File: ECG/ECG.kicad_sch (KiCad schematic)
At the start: 91 parts, among them J1 Conn_01x03, J10 Socket 1x15, J11 Shunt block, J12 Shunt block, J13 Shunt block, J14 Shunt block, J15 Shunt block, J16 Shunt block, J17 Conn_02x04_Odd_Even, J2 Conn_01x03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

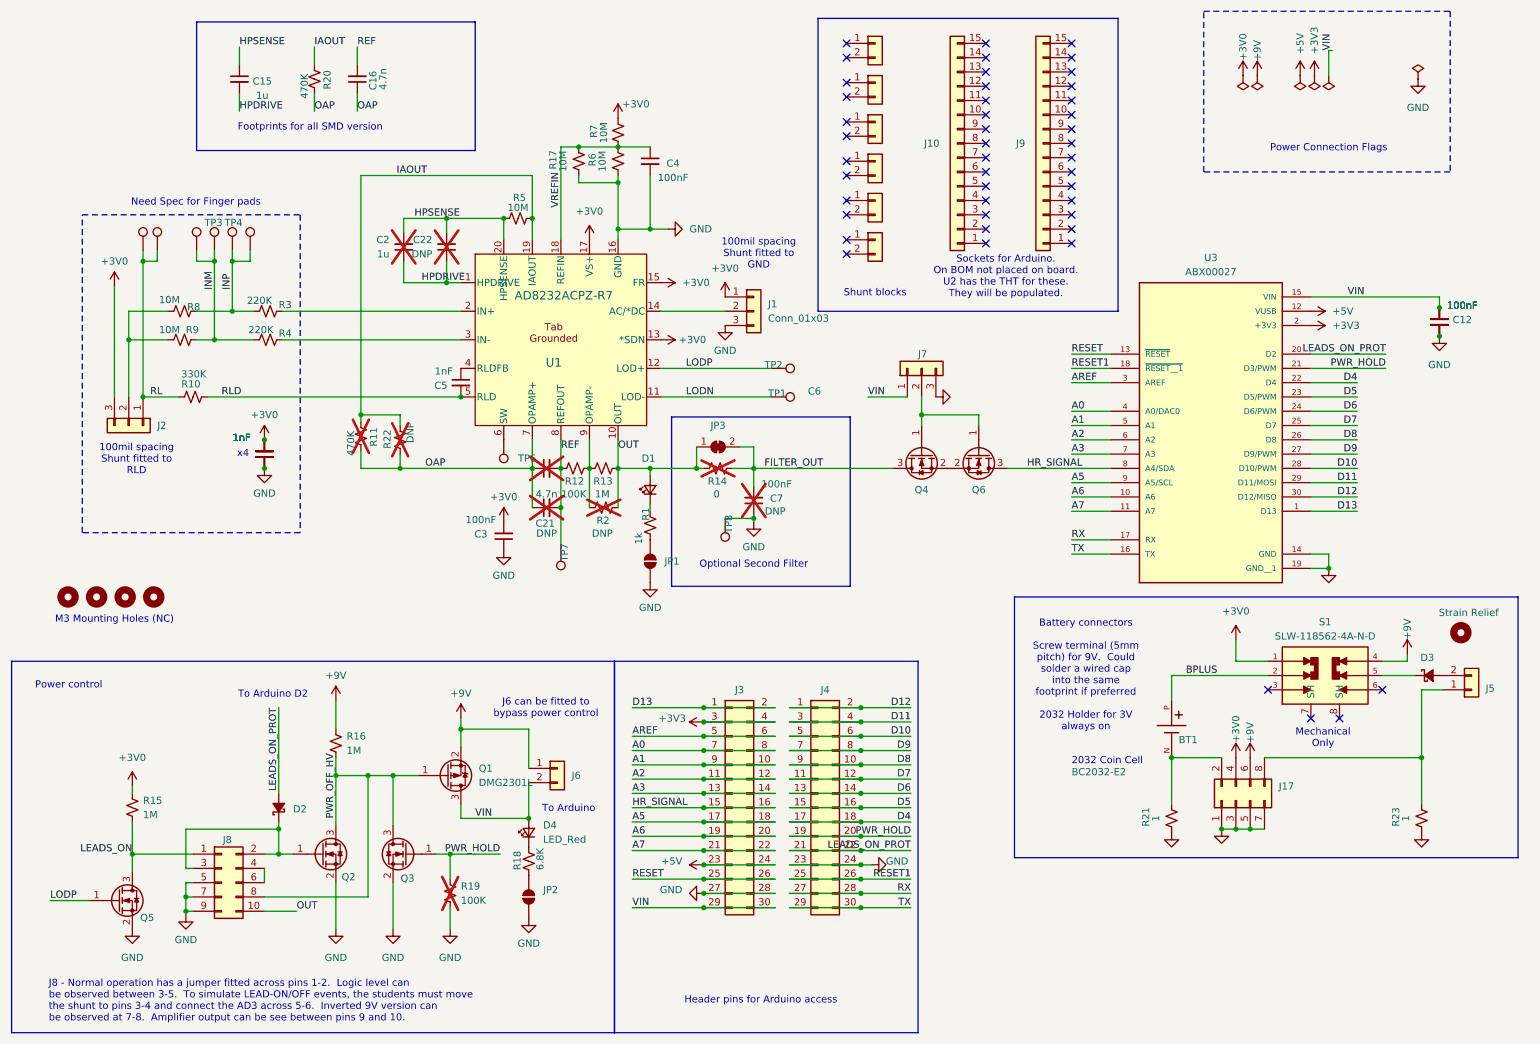
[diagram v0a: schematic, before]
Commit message: Add op amp buffer to pwr_off_hv to allow monitoring with the relatively low input impedance of the AD3
Work on #25

Probably need to look for a CMOS op-amp.  This one pulls
600nA input bias which will likely turn on the pfet and
power up the nano all the time...
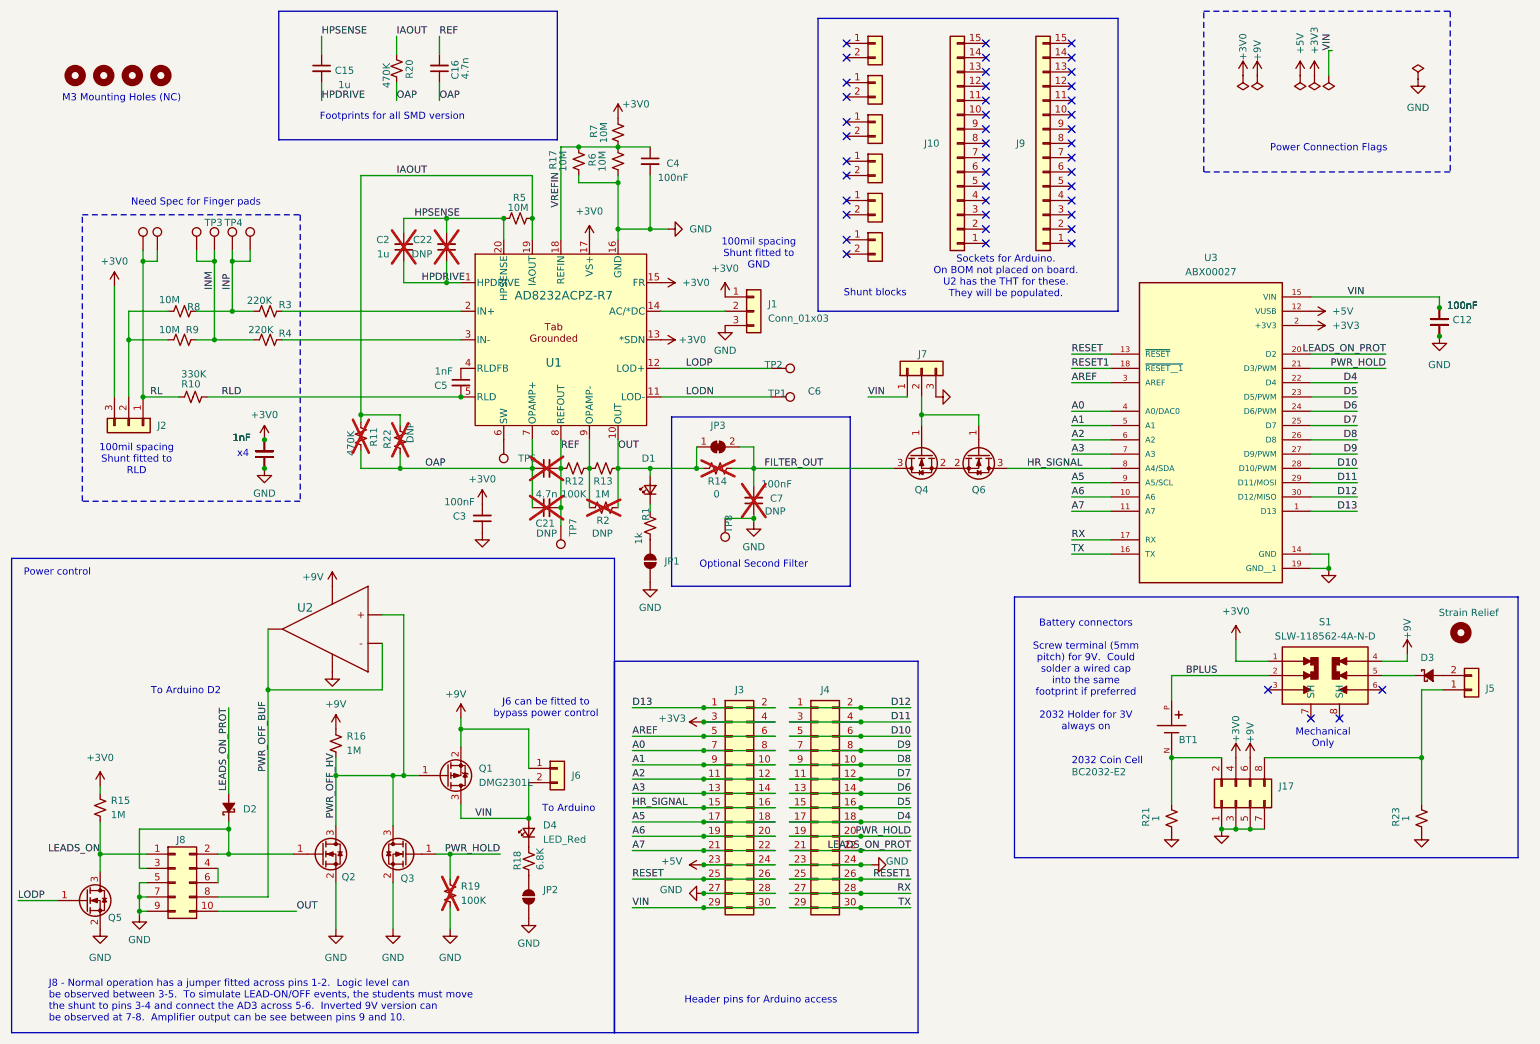
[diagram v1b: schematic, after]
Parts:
- added U2: MIC920YC5-TR, StockedComponents:SC-70_C5_MCH, symbol StockedComponents:MIC920YC5-TR
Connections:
- net +9V: now also U2.5 (V+)
- net GND: now also U2.2 (V-)
- net PWR_OFF_HV: now also U2.1 (IN+); no longer J8.8 (Pin_8)
- new net PWR_OFF_BUF: J8.8 (Pin_8), U2.3 (IN-), U2.4 (OUT)
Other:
- moved on the sheet: C15, C16, C3, D2, J8, Q5, R15, R20, TP7

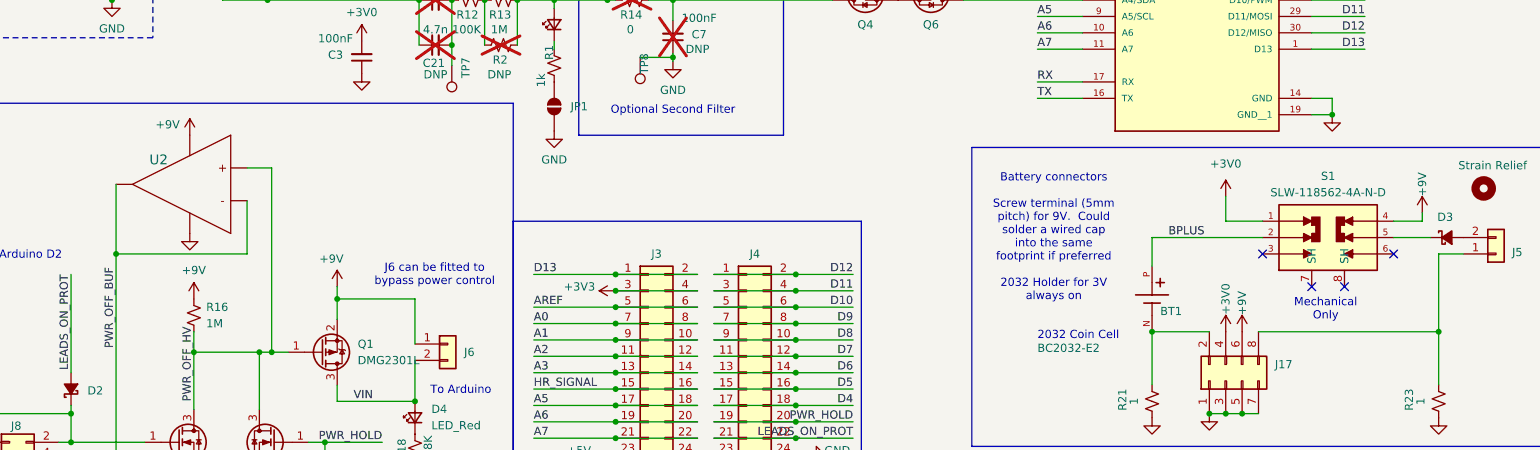
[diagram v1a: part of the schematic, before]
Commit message: Start looking at footprints and placements.
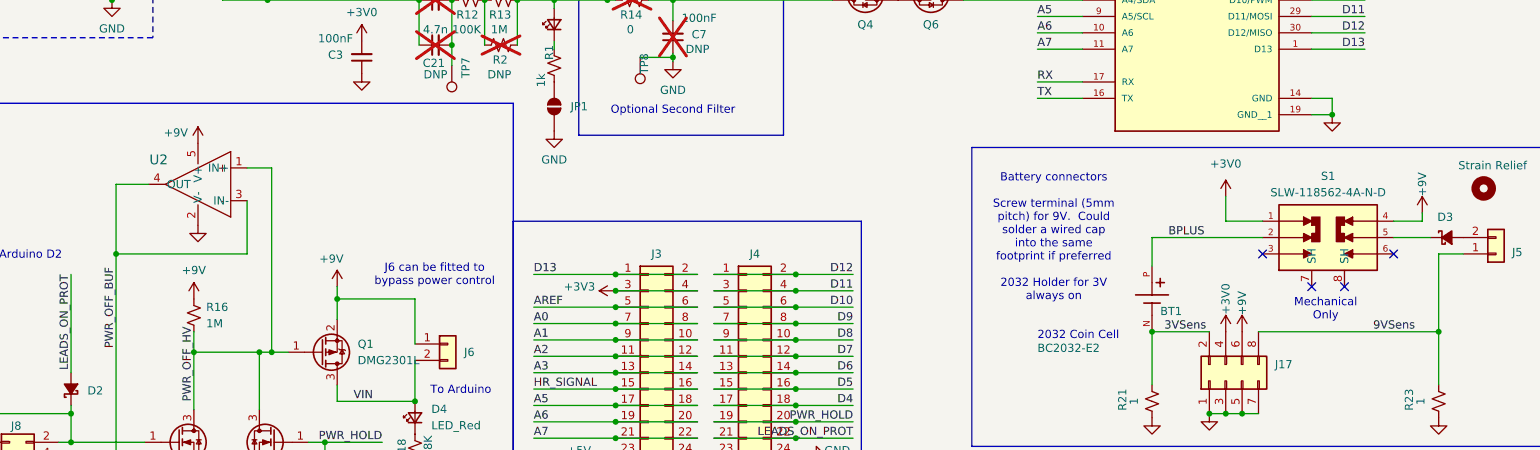
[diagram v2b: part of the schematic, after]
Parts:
- J17: footprint (none) -> Connector_PinHeader_2.54mm:PinHeader_2x04_P2.54mm_Vertical
- J3, J4: footprint (none) -> Connector_PinHeader_2.54mm:PinHeader_2x15_P2.54mm_Vertical
- U2: footprint StockedComponents:SC-70_C5_MCH -> SC-70_C5_MCH
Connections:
- net 9VSens: now reaches J17.8 (Pin_8), J5.1 (Pin_1), R23.1
- net 3VSens: now reaches BT1.N, J17.2 (Pin_2), R21.1
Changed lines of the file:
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@@
 	(wire
 		(pts
+			(xy 61.595 123.825) (xy 66.675 123.825)
+		)
+		(stroke
+			(width 0)
+			(type default)
+		)
+	)
+	(wire
+		(pts
 			(xy 38.735 168.91) (xy 40.005 168.91)
 		)
@@
 		)
 	)
+	(label "9VSens"
+		(at 256.54 146.685 0)
+		(effects
+			(font
+				(size 1.27 1.27)
+			)
+			(justify left bottom)
+		)
+	)
 	(label "RL"
 		(at 40.64 82.55 0)
@@
 		)
 	)
+	(label "3VSens"
+		(at 224.155 146.685 0)
+		(effects
+			(font
+				(size 1.27 1.27)
+			)
+			(justify left bottom)
+		)
+	)
 	(label "PWR_HOLD"
 		(at 260.35 77.47 180)
@@
 			)
 		)
-		(property "Footprint" ""
+		(property "Footprint" "Connector_PinHeader_2.54mm:PinHeader_2x15_P2.54mm_Vertical"
 			(at 144.145 155.575 0)
 			(effects
@@
 			)
 		)
-		(property "Footprint" ""
+		(property "Footprint" "Connector_PinHeader_2.54mm:PinHeader_2x04_P2.54mm_Vertical"
 			(at 233.68 154.305 0)
 			(effects
@@
 	(symbol
 		(lib_id "power:+9V")
-		(at 73.025 116.205 0)
+		(at 74.295 117.475 0)
 		(mirror y)
 		(unit 1)
@@
 		(dnp no)
 		(property "Reference" "#PWR045"
-			(at 73.025 120.015 0)
+			(at 74.295 121.285 0)
 			(effects
 				(font
@@
 		)
 		(property "Value" "+9V"
-			(at 69.596 114.554 0)
+			(at 70.866 115.824 0)
 			(effects
 				(font
@@
 		)
 		(property "Footprint" ""
-			(at 73.025 116.205 0)
+			(at 74.295 117.475 0)
 			(effects
 				(font
@@
 		)
 		(property "Datasheet" ""
-			(at 73.025 116.205 0)
+			(at 74.295 117.475 0)
 			(effects
 				(font
@@
 		)
 		(property "Description" "Power symbol creates a global label with name \"+9V\""
-			(at 73.025 116.205 0)
+			(at 74.295 117.475 0)
 			(effects
 				(font
@@
 			)
 		)
-		(property "Footprint" "StockedComponents:SC-70_C5_MCH"
+		(property "Footprint" "SC-70_C5_MCH"
 			(at 86.995 121.285 0)
 			(effects
@@
 	(symbol
 		(lib_id "power:GND")
-		(at 73.025 131.445 0)
+		(at 74.295 130.175 0)
 		(unit 1)
 		(exclude_from_sim no)
@@
 		(fields_autoplaced yes)
 		(property "Reference" "#PWR046"
-			(at 73.025 137.795 0)
+			(at 74.295 136.525 0)
 			(effects
 				(font
@@
 		)
 		(property "Value" "GND"
-			(at 73.025 135.89 0)
+			(at 74.295 134.62 0)
 			(effects
 				(font
@@
 		)
 		(property "Footprint" ""
-			(at 73.025 131.445 0)
+			(at 74.295 130.175 0)
 			(effects
 				(font
@@
 		)
 		(property "Datasheet" ""
-			(at 73.025 131.445 0)
+			(at 74.295 130.175 0)
 			(effects
 				(font
@@
 		)
 		(property "Description" "Power symbol creates a global label with name \"GND\" , ground"
-			(at 73.025 131.445 0)
+			(at 74.295 130.175 0)
 			(effects
 				(font
@@
 			)
 		)
-		(property "Footprint" ""
+		(property "Footprint" "Connector_PinHeader_2.54mm:PinHeader_2x15_P2.54mm_Vertical"
 			(at 159.385 155.575 0)
 			(effects
